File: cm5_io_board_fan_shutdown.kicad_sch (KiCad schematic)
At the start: 31 parts, among them J1 Conn_Pi_JST_SH, J2 Conn_Fan_JST_SH, J3 Conn_Fan_Header, Q1 AO3401A, Q2 BSS138, Q3 BSS138, U1 LM393

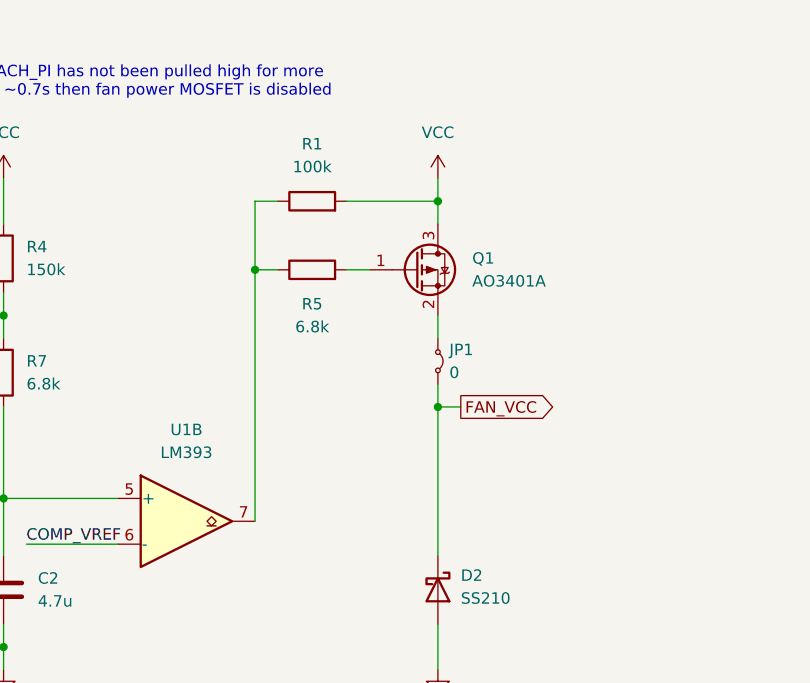
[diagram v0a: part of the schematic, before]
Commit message: [fix_output_drive] flipped output FET, added voltage divider in output driver schematic
Output P-FET has been flipped so it should no longer conduct through body diode when off, gate resistor has been changed to form voltage divider with pullup to limit VGS to ~10V when operating from 12Vcc as VGSmax is +-12V
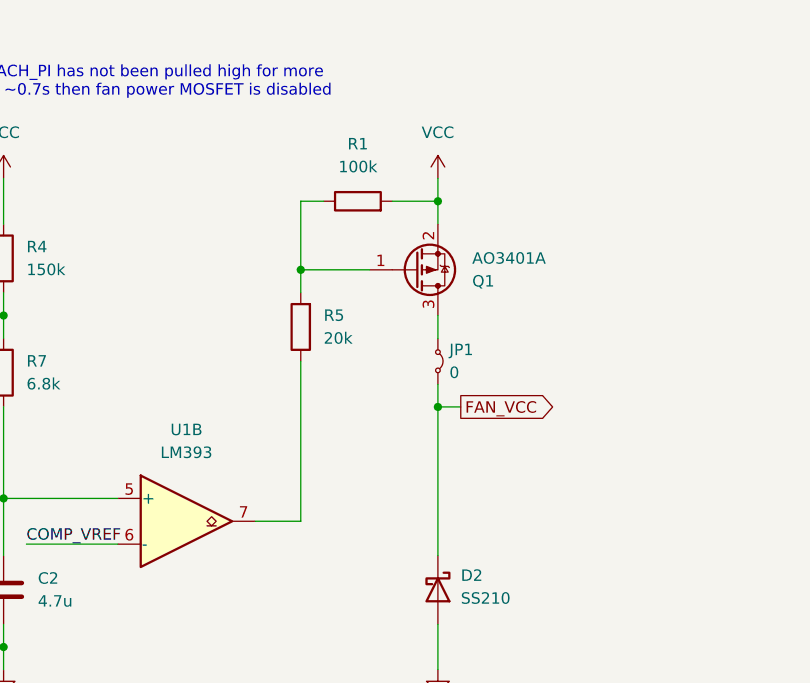
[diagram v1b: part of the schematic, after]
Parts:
- R5: value 6.8k -> 20k
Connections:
- net VCC: now also Q1.2 (S); no longer Q1.3 (D)
- net at R5.1, U1.7: no longer R1.1
- net at Q1.1 (G), R5.2: now also R1.1
- net at JP1.1 (A): now also Q1.3 (D); no longer Q1.2 (S)
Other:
- moved on the sheet: R1, R5
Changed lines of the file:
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@@
 	)
 	(junction
-		(at 210.82 58.42)
+		(at 215.9 58.42)
 		(diameter 0)
 		(color 0 0 0 0)
@@
 	(wire
 		(pts
-			(xy 210.82 50.8) (xy 213.36 50.8)
+			(xy 215.9 50.8) (xy 218.44 50.8)
 		)
 		(stroke
@@
 	(wire
 		(pts
-			(xy 210.82 58.42) (xy 210.82 86.36)
+			(xy 215.9 86.36) (xy 210.82 86.36)
+		)
+		(stroke
+			(width 0)
+			(type default)
+		)
+	)
+	(wire
+		(pts
+			(xy 215.9 58.42) (xy 215.9 60.96)
 		)
 		(stroke
@@
 	(wire
 		(pts
+			(xy 215.9 68.58) (xy 215.9 86.36)
+		)
+		(stroke
+			(width 0)
+			(type default)
+		)
+	)
+	(wire
+		(pts
 			(xy 125.73 78.74) (xy 128.27 78.74)
 		)
@@
 	(wire
 		(pts
-			(xy 210.82 58.42) (xy 213.36 58.42)
+			(xy 215.9 58.42) (xy 223.52 58.42)
 		)
 		(stroke
@@
 	(wire
 		(pts
-			(xy 220.98 58.42) (xy 223.52 58.42)
-		)
-		(stroke
-			(width 0)
-			(type default)
-		)
-	)
-	(wire
-		(pts
 			(xy 210.82 143.51) (xy 210.82 148.59)
 		)
@@
 	(wire
 		(pts
-			(xy 210.82 58.42) (xy 210.82 50.8)
+			(xy 215.9 58.42) (xy 215.9 50.8)
 		)
 		(stroke
@@
 	(wire
 		(pts
-			(xy 220.98 50.8) (xy 231.14 50.8)
+			(xy 226.06 50.8) (xy 231.14 50.8)
 		)
 		(stroke
@@
 	(symbol
 		(lib_id "Device:R")
-		(at 217.17 58.42 90)
+		(at 215.9 64.77 180)
 		(unit 1)
 		(exclude_from_sim no)
@@
 		(fields_autoplaced yes)
 		(property "Reference" "R5"
-			(at 217.17 62.23 90)
+			(at 218.44 63.4999 0)
 			(effects
 				(font
 					(size 1.27 1.27)
 				)
+				(justify right)
 			)
 		)
-		(property "Value" "6.8k"
-			(at 217.17 64.77 90)
+		(property "Value" "20k"
+			(at 218.44 66.0399 0)
 			(effects
 				(font
 					(size 1.27 1.27)
 				)
+				(justify right)
 			)
 		)
 		(property "Footprint" "Resistor_SMD:R_0603_1608Metric"
-			(at 217.17 60.198 90)
+			(at 217.678 64.77 90)
 			(effects
 				(font
@@
 		)
 		(property "Datasheet" "~"
-			(at 217.17 58.42 0)
+			(at 215.9 64.77 0)
 			(effects
 				(font
@@
 		)
 		(property "Description" "Resistor"
-			(at 217.17 58.42 0)
+			(at 215.9 64.77 0)
 			(effects
 				(font
@@
 	(symbol
 		(lib_id "Device:R")
-		(at 217.17 50.8 90)
+		(at 222.25 50.8 90)
 		(unit 1)
 		(exclude_from_sim no)
@@
 		(fields_autoplaced yes)
 		(property "Reference" "R1"
-			(at 217.17 44.45 90)
+			(at 222.25 44.45 90)
 			(effects
 				(font
@@
 		)
 		(property "Value" "100k"
-			(at 217.17 46.99 90)
+			(at 222.25 46.99 90)
 			(effects
 				(font
@@
 		)
 		(property "Footprint" "Resistor_SMD:R_0603_1608Metric"
-			(at 217.17 52.578 90)
+			(at 222.25 52.578 90)
 			(effects
 				(font
@@
 		)
 		(property "Datasheet" "~"
-			(at 217.17 50.8 0)
+			(at 222.25 50.8 0)
 			(effects
 				(font
@@
 		)
 		(property "Description" "Resistor"
-			(at 217.17 50.8 0)
+			(at 222.25 50.8 0)
 			(effects
 				(font
@@
 		(lib_id "Transistor_FET:AO3401A")
 		(at 228.6 58.42 0)
+		(mirror x)
 		(unit 1)
 		(exclude_from_sim no)
@@
 		(on_board yes)
 		(dnp no)
-		(fields_autoplaced yes)
 		(property "Reference" "Q1"
-			(at 234.95 57.1499 0)
+			(at 234.95 59.6901 0)
 			(effects
 				(font
@@
 		)
 		(property "Value" "AO3401A"
-			(at 234.95 59.6899 0)
+			(at 234.95 57.1501 0)
 			(effects
 				(font
@@
 		)
 		(property "Footprint" "Package_TO_SOT_SMD:SOT-23"
-			(at 233.68 60.325 0)
+			(at 233.68 56.515 0)
 			(effects
 				(font
@@
 		)
 		(property "Datasheet" "http://www.aosmd.com/pdfs/datasheet/AO3401A.pdf"
-			(at 233.68 62.23 0)
+			(at 233.68 54.61 0)
 			(effects
 				(font
